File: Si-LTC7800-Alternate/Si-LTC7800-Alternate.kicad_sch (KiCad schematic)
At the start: 40 parts, among them Q1 EPC2014C, Q2 EPC2014C, U1 LTC7800HUDC_PBF

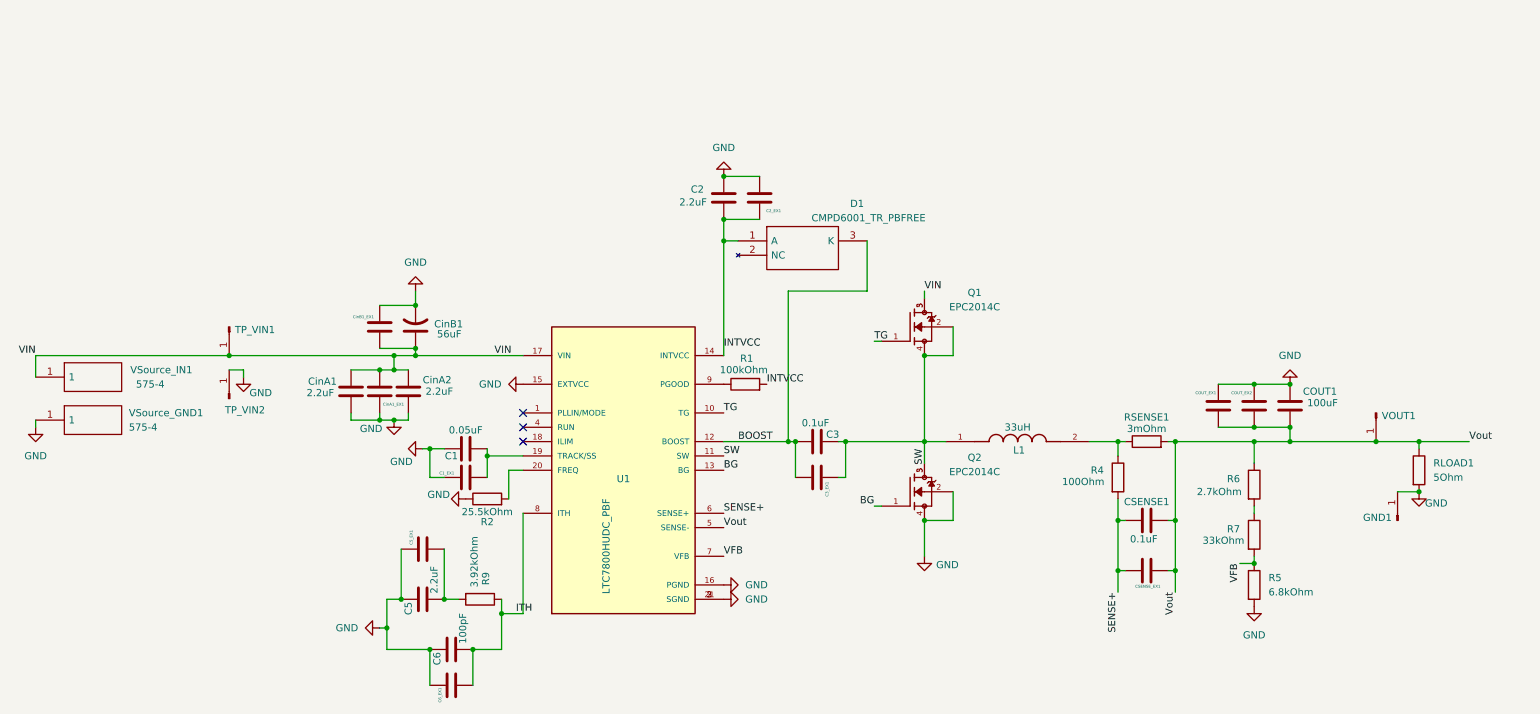
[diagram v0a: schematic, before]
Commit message: new GaN switches, added alt projects
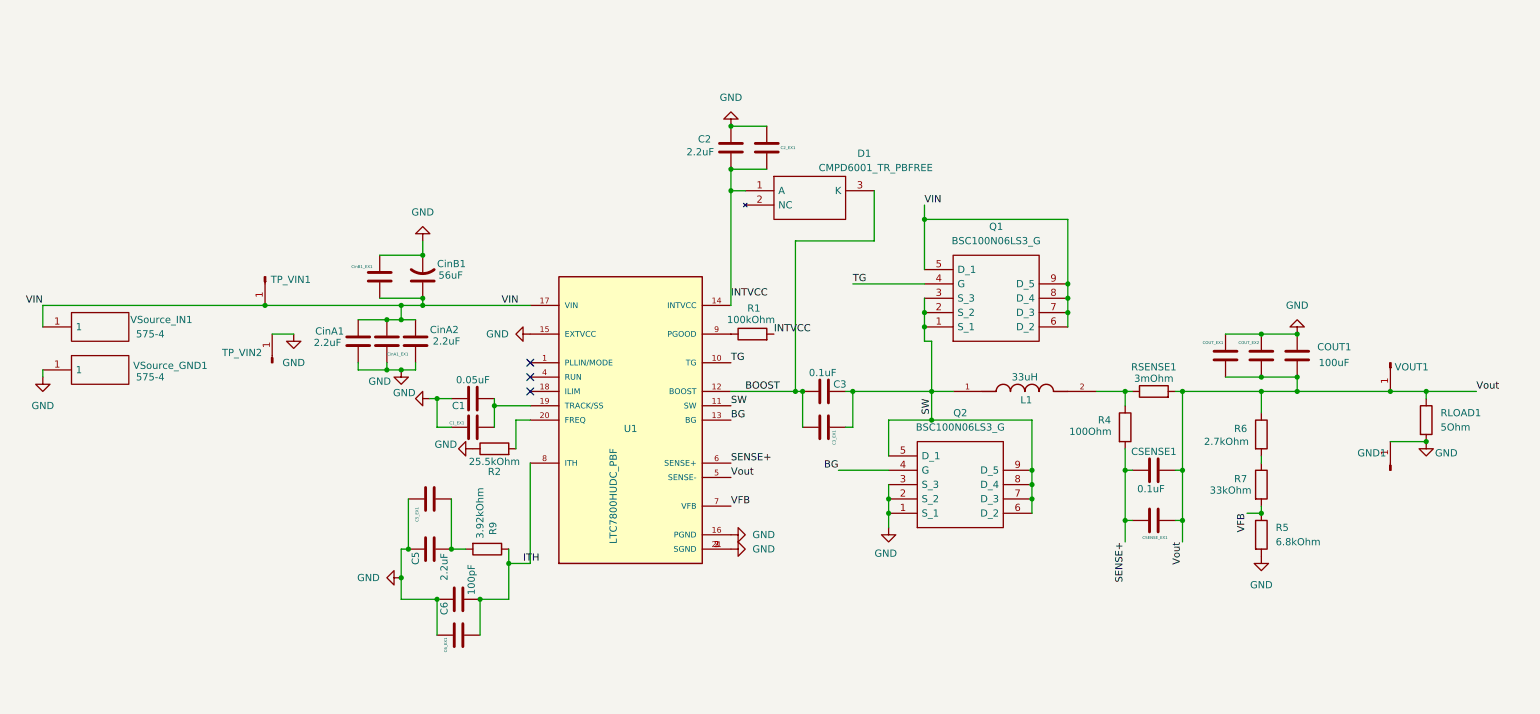
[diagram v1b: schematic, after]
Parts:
- removed Q1, Q2: EPC2014C, XT60PW-M:TRANS_EPC2014C, symbol EPC2014C:EPC2014C
- added Q1, Q2: BSC100N06LS3_G, Transistor_Power:BSC100N06LS3G, symbol BSC100N06LS3_G:BSC100N06LS3_G
- U1: footprint Package_DFN_QFN:QFN50P400X300X80-21N -> Library:QFN50P400X300X80-21N
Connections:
- net BG: now also Q2.4 (G)
- net GND: now also Q2.1 (S_1), Q2.2 (S_2), Q2.3 (S_3)
- net SW: now also Q1.1 (S_1), Q1.2 (S_2), Q1.3 (S_3), Q2.5 (D_1), Q2.6 (D_2), Q2.7 (D_3), Q2.8 (D_4), Q2.9 (D_5)
- net TG: now also Q1.4 (G)
- net VIN: now also Q1.5 (D_1), Q1.6 (D_2), Q1.7 (D_3), Q1.8 (D_4), Q1.9 (D_5)
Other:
- moved on the sheet: C1, C1_EX1, C2, C2_EX1, C3, C3_EX1, C5, C5_EX1, C6, C6_EX1, COUT1, COUT_EX1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

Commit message: Updating PCBs for preassembly
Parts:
- added RLOAD2: 2Ohm, Resistor_SMD:R_0201_0603Metric, symbol Device:R
- C1, C3, CSENSE1: footprint Capacitor_SMD:C_0805_2012Metric_Pad1.18x1.45mm_HandSolder -> Capacitor_SMD:C_0805_2012Metric; LCSC (none) -> C49678
- C2, C5, CinA1, CinA2: footprint Capacitor_SMD:C_0805_2012Metric_Pad1.18x1.45mm_HandSolder -> Capacitor_SMD:C_0805_2012Metric; LCSC (none) -> C19110
- C6: footprint Capacitor_SMD:C_0805_2012Metric_Pad1.18x1.45mm_HandSolder -> Capacitor_SMD:C_0805_2012Metric; LCSC (none) -> C1970
- COUT1: footprint Capacitor_SMD:C_0805_2012Metric_Pad1.18x1.45mm_HandSolder -> Capacitor_SMD:C_0805_2012Metric; LCSC (none) -> C141660
- CinB1: footprint Capacitor_SMD:C_0805_2012Metric_Pad1.18x1.45mm_HandSolder -> Capacitor_Tantalum_SMD:CP_EIA-7343-31_Kemet-D; LCSC (none) -> C465937
- D1: LCSC (none) -> C17357273
- Q1, Q2: LCSC (none) -> C72767
- R1: footprint Resistor_SMD:R_0201_0603Metric_Pad0.64x0.40mm_HandSolder -> Resistor_SMD:R_0201_0603Metric; LCSC (none) -> C14675
- R2: footprint Resistor_SMD:R_0201_0603Metric_Pad0.64x0.40mm_HandSolder -> Resistor_SMD:R_0201_0603Metric; LCSC (none) -> C861257
- R4: footprint Resistor_SMD:R_0201_0603Metric_Pad0.64x0.40mm_HandSolder -> Resistor_SMD:R_0201_0603Metric; LCSC (none) -> C105588
- R5: footprint Resistor_SMD:R_0201_0603Metric_Pad0.64x0.40mm_HandSolder -> Resistor_SMD:R_0201_0603Metric; LCSC (none) -> C2907055
- R6: footprint Resistor_SMD:R_0201_0603Metric_Pad0.64x0.40mm_HandSolder -> Resistor_SMD:R_0201_0603Metric; LCSC (none) -> C2907008
- R7: footprint Resistor_SMD:R_0201_0603Metric_Pad0.64x0.40mm_HandSolder -> Resistor_SMD:R_0201_0603Metric; LCSC (none) -> C2907028
- R9: footprint Resistor_SMD:R_0201_0603Metric_Pad0.64x0.40mm_HandSolder -> Resistor_SMD:R_0201_0603Metric; LCSC (none) -> C4168160
- RLOAD1: value 5Ohm -> 3Ohm; footprint Resistor_SMD:R_0201_0603Metric_Pad0.64x0.40mm_HandSolder -> Resistor_SMD:R_0201_0603Metric; LCSC (none) -> C23157
- RSENSE1: footprint Resistor_SMD:R_0201_0603Metric_Pad0.64x0.40mm_HandSolder -> Resistor_SMD:R_0201_0603Metric; LCSC (none) -> C7256520
- U1: LCSC (none) -> C690192
- VSource_GND1, VSource_IN1: LCSC (none) -> C4944061
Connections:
- net GND: now also RLOAD2.2; no longer RLOAD1.2
- new net: RLOAD1.2, RLOAD2.1
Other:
- moved on the sheet: C1, C1_EX1, C2, C2_EX1, C3, C3_EX1, C5, C5_EX1, C6, C6_EX1, COUT1, COUT_EX1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
